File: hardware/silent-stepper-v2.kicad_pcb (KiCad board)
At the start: 4 copper layers, 80 x 80 mm, 112 parts, among them P1 VIN, P101 CON-SENSOR2, P102 DEBUG, P103 BOOT, P2 OUT, P3 GPIO, P4 PROTO, Q1 CSD19533Q5A, Q2 CSD19533Q5A, Q3 CSD19533Q5A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

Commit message: changed resistor
Signed-off-by: Tim Schneidermann <tim@tinkerforge.com>
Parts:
- moved C25 1.50 mm to (59.7, 142.2)
- moved R22 1.50 mm to (59.7, 143.7)
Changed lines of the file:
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@@
-(kicad_pcb (version 20171130) (host pcbnew 5.1.5-52549c5~84~ubuntu19.04.1)
+(kicad_pcb (version 20171130) (host pcbnew "(5.1.4)-1")
   (general
     (thickness 1.6)
@@
     (aux_axis_origin 45 90)
     (grid_origin 45 90)
-    (visible_elements FFFFFF7F)
+    (visible_elements 7FFFFFFF)
     (pcbplotparams
       (layerselection 0x010fc_ffffffff)
@@
   )
   (module kicad-libraries:C0603F (layer F.Cu)
-    (at 59.7 143.7 180)
+    (at 59.7 142.2 180)
     (attr smd)
     (fp_text reference C25 (at 0.05 0.225) (layer F.Fab)
@@
   )
   (module kicad-libraries:R0603F (layer F.Cu)
-    (at 59.7 142.2)
+    (at 59.7 143.7)
     (attr smd)
     (fp_text reference R22 (at 0.05 0.225) (layer F.Fab)

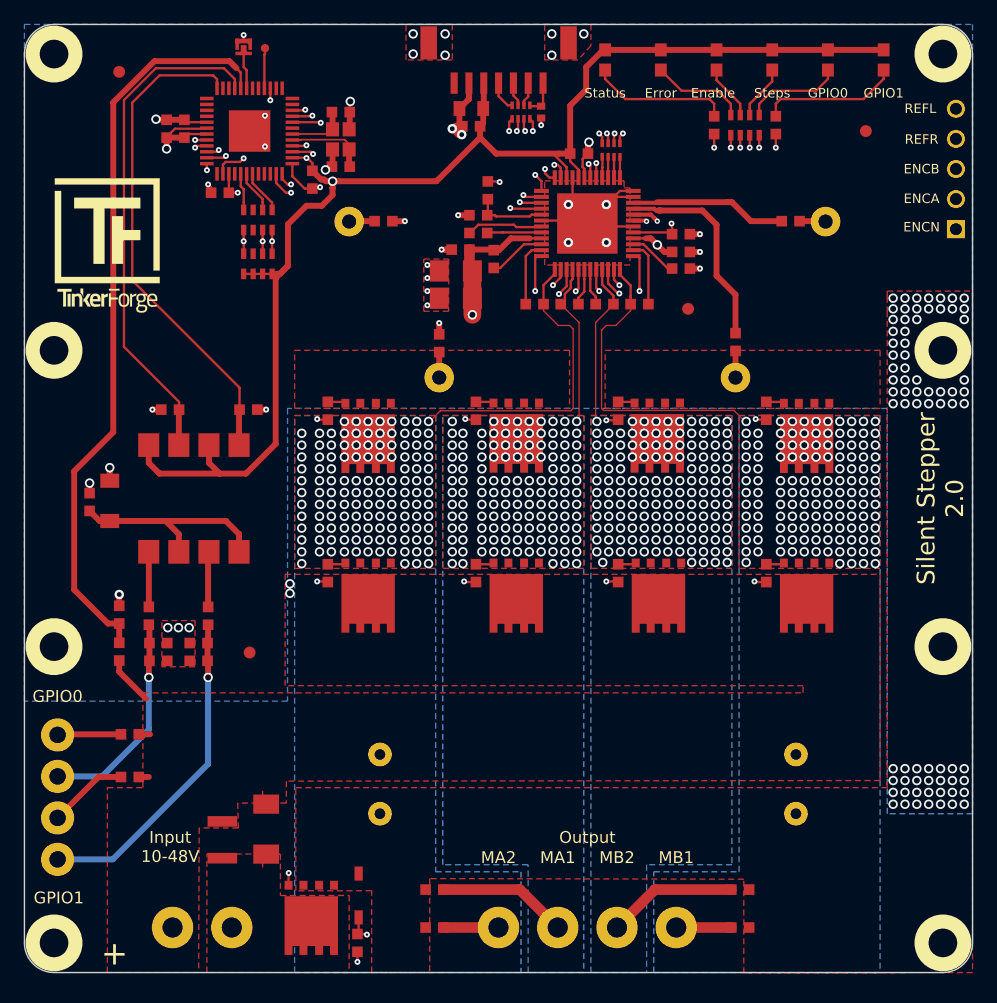
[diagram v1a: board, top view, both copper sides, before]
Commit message: added Temperature Sensor, added pullups and ground to proto header, removed screwholes, moved 47 ohm inline resitors for better shunt clearance, removed no-silkscreen area on bottomlayer, removed big tinkerforge logo on bottomlayer
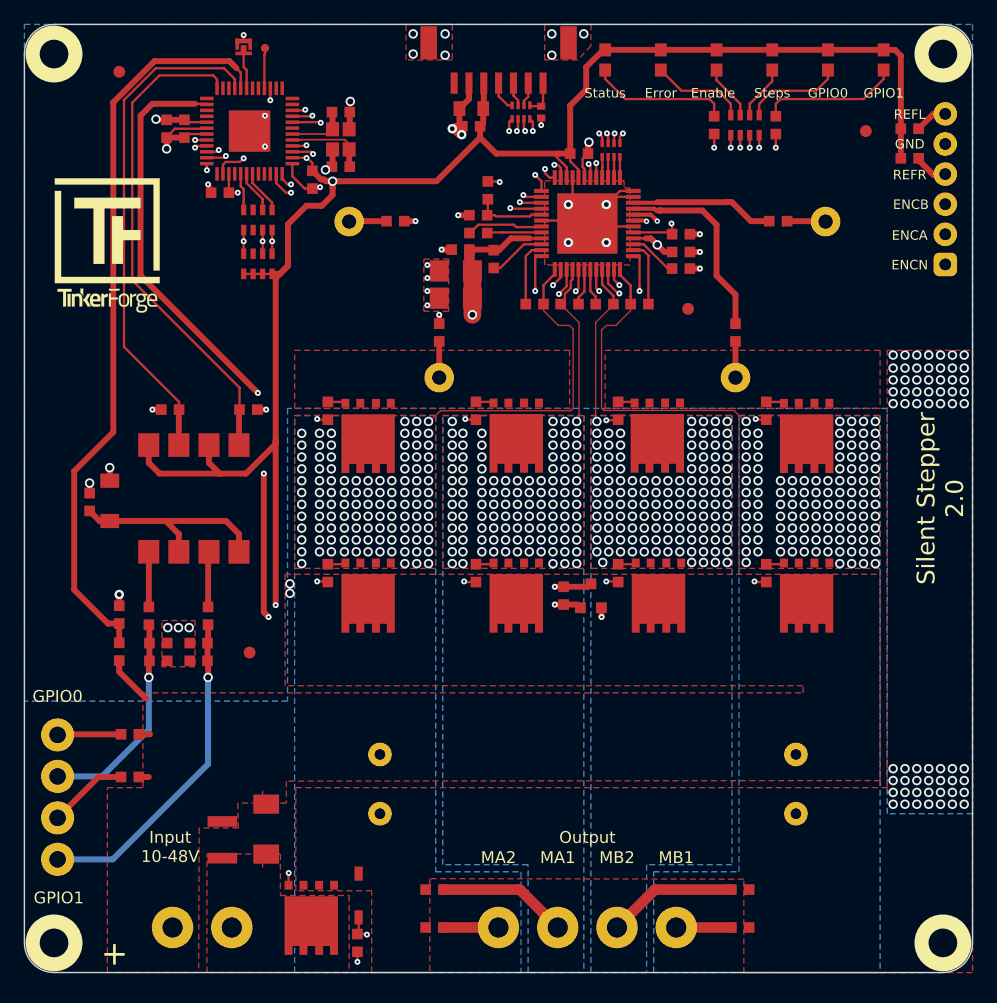
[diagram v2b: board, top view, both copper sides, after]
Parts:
- removed the G*** at (85.0, 103.5)
- removed U5, U6, U7: DRILL, kicad-libraries:DRILL_NP
- added C19: 100nF, kicad-libraries:C0603F, F.Cu at (90.5, 138.2)
- added R30: DNP, kicad-libraries:R0603F, F.Cu at (119.7, 98.8)
- added R31: DNP, kicad-libraries:R0603F, F.Cu at (119.7, 101.3)
- P4: footprint kicad-libraries:pin_array_5x1 -> kicad-libraries:pin_array_1x6-P2mm_D1mm
- U4: value DRILL -> TMP235; footprint kicad-libraries:DRILL_NP -> kicad-libraries:SOT23-3
- moved U4 45.5 mm to (92.8, 138.2), turned to 180 degrees
- moved P4 1.92 mm to (122.7, 103.9)
- moved R7 1.05 mm to (108.6, 106.6)
- moved R9 1.00 mm to (76.3, 106.6)
- moved R8 0.90 mm to (80.0, 116.0)
- moved R6 0.80 mm to (105.0, 116.0)
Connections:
- P4 pad 5: Net-(P4-Pad5) -> GND
- U1 pad 17: Net-(P4-Pad5) -> Net-(P4-Pad6)
- U2 pad 14: Net-(U2-Pad14) -> TEMP
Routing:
- net TEMP: track 0.00 -> 82.2 mm, vias 0 -> 4
- net VCC: track 150.7 -> 200.9 mm, vias 4 -> 6
- net Net-(P4-Pad6): track 0.00 -> 35.2 mm, vias 0 -> 1
- net Net-(P4-Pad5): track 33.5 -> 0.00 mm, vias 1 -> 0
- net GND: track 61.5 -> 66.7 mm, vias 112 -> 104
- net Net-(P4-Pad4): track 33.5 -> 34.6 mm
- net Net-(R7-Pad2): track 13.2 -> 12.2 mm
- net Net-(R9-Pad2): track 22.8 -> 21.8 mm
- net Net-(Q4-PadS): track 2.15 -> 3.05 mm
- net Net-(R6-Pad2): track 17.6 -> 16.8 mm
- net Net-(Q2-PadS): track 2.25 -> 3.05 mm
- net Net-(C16-Pad1): vias 130 -> 110
- net Net-(C15-Pad1): vias 128 -> 108
- net Net-(C14-Pad1): vias 131 -> 111
- net Net-(C13-Pad1): vias 142 -> 122
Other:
- board text added: "GND"

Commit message: changed resistor array footprint
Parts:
- R10: value MRS-3 -> .
- R11: value MRS_-3 -> .
- RP2: footprint kicad-libraries:4X0402 -> kicad-libraries:4X0603
- moved RP2 0.89 mm to (95.3, 100.2), turned to 0 degrees
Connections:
- RP2 pad 1: CS_TMC -> MISO_TMC
- RP2 pad 2: SCK_TMC -> MOSI_TMC
- RP2 pad 3: MOSI_TMC -> SCK_TMC
- RP2 pad 4: MISO_TMC -> CS_TMC
- U1 pad 13: Net-(RP2-Pad8) -> Net-(RP2-Pad5)
- U1 pad 14: Net-(RP2-Pad7) -> Net-(RP2-Pad6)
- U1 pad 15: Net-(RP2-Pad6) -> Net-(RP2-Pad7)
- U1 pad 16: Net-(RP2-Pad5) -> Net-(RP2-Pad8)
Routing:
- net CS_TMC: track 31.1 -> 32.6 mm
- net SCK_TMC: track 29.9 -> 31.3 mm
- net MOSI_TMC: track 31.3 -> 32.4 mm
- net Net-(RP2-Pad5): track 1.77 -> 2.64 mm
- net MISO_TMC: track 31.4 -> 32.2 mm
- net Net-(RP2-Pad6): track 1.75 -> 2.47 mm

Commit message: new hardware version
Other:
- board text added: "Silent Stepper 2.1"
- board text removed: "Silent Stepper 2.0"
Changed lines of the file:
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@@
-(kicad_pcb (version 20171130) (host pcbnew 5.1.6-c6e7f7d~86~ubuntu20.04.1)
+(kicad_pcb (version 20171130) (host pcbnew 5.1.6-c6e7f7d~87~ubuntu20.04.1)
   (general
     (thickness 1.6)
@@
     (effects (font (size 0.8 0.8) (thickness 0.15)))
   )
-  (gr_text "Silent Stepper\n2.0" (at 122.3 130 90) (layer F.SilkS)
+  (gr_text "Silent Stepper\n2.1" (at 122.3 130 90) (layer F.SilkS)
     (effects (font (size 1.5 1.5) (thickness 0.25)))
   )

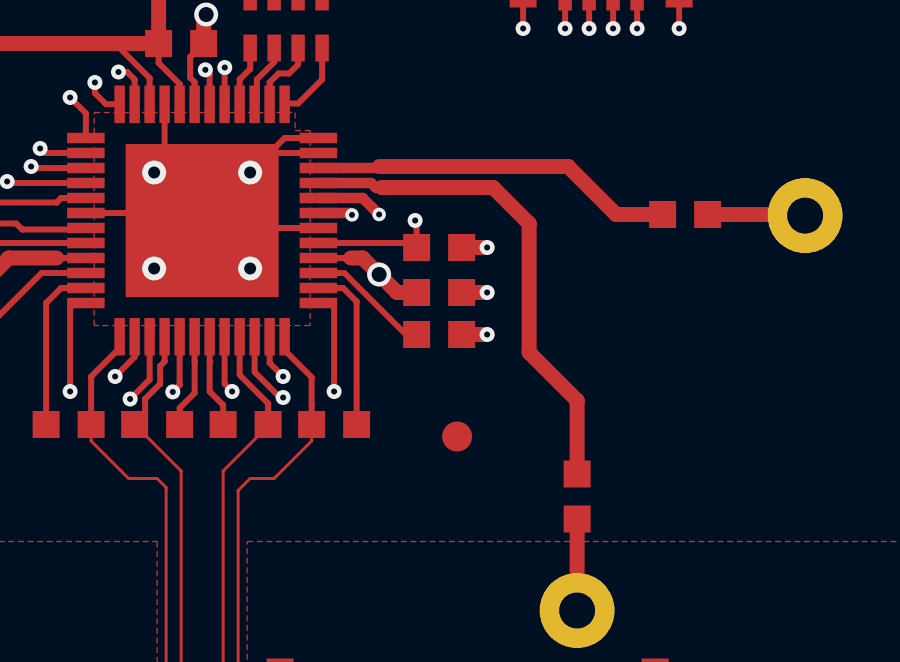
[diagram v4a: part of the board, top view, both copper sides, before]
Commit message: changed C6, C7 footprint to 0805 and updated SON_5x6 footprint
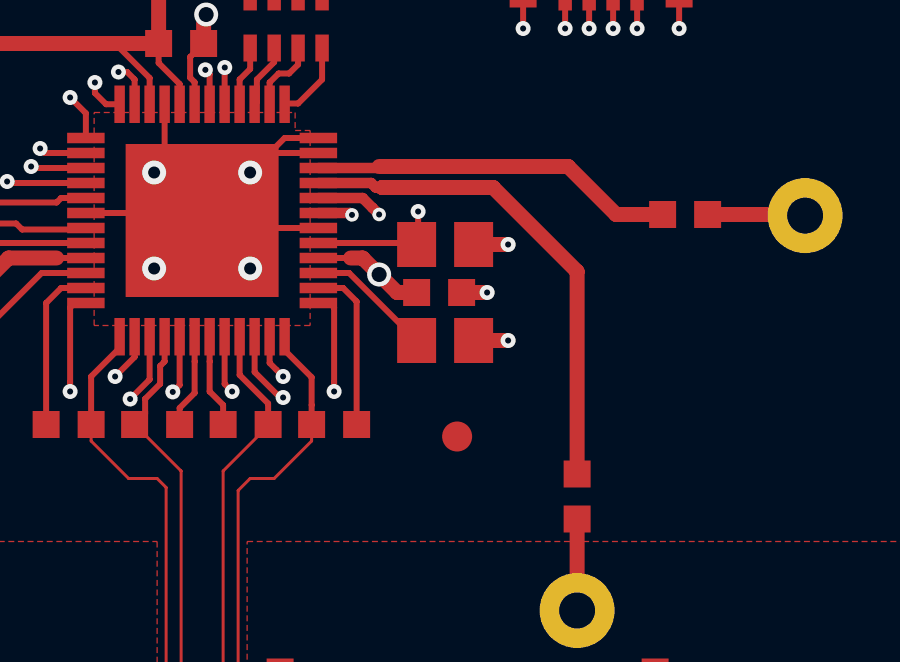
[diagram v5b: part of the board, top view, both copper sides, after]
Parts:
- C23, C24, C25: value 100nF -> 100nF/100V
- C6, C7: footprint kicad-libraries:C0603F -> kicad-libraries:C0805E
- C9: value 100nF/100V -> 100nF
- moved C6 0.28 mm to (100.6, 110.8)
- moved C7 0.22 mm to (100.6, 107.6)
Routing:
- net GND: track 66.7 -> 67.3 mm
